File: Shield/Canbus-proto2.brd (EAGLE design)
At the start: 92.8 x 53 mm, 81 parts, among them J1 Digital_0_7, J2 Analog, J3 Digital_8_13, J4 Analog, J5 Digital_14_21

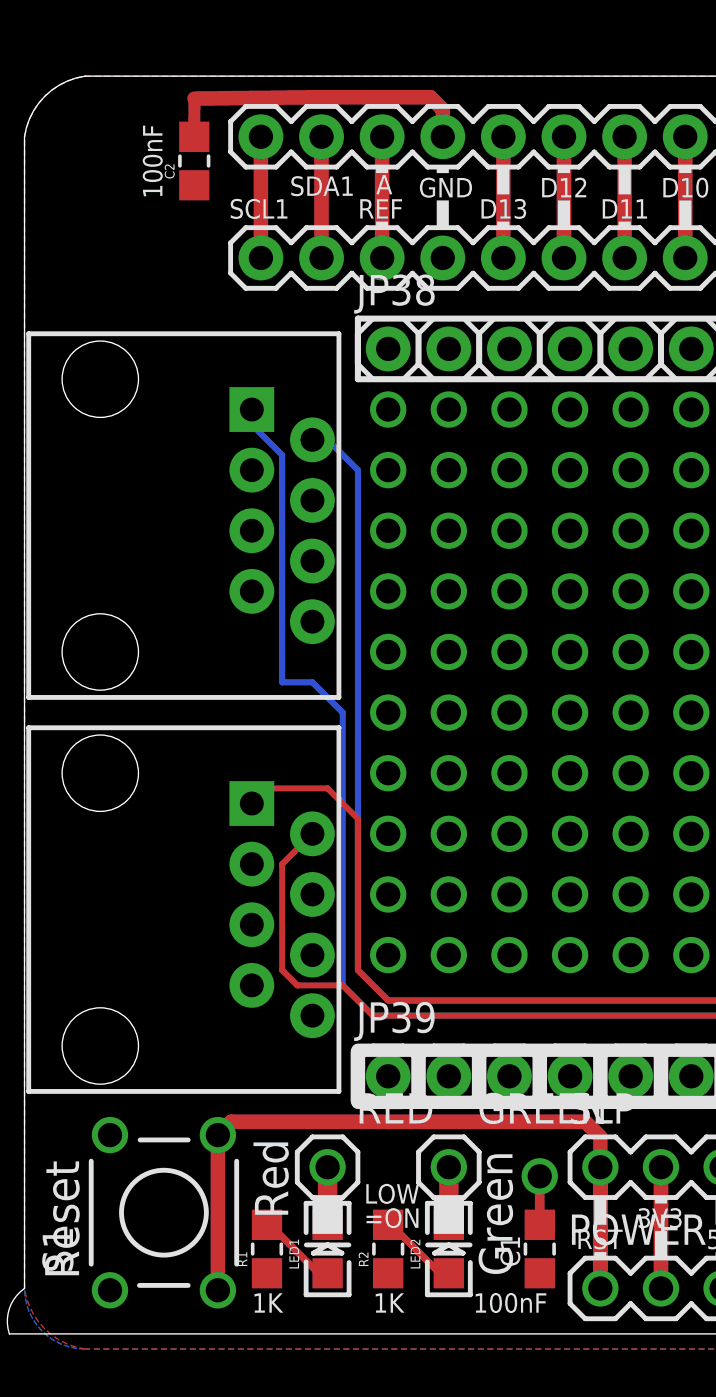
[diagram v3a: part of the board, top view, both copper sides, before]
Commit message: Switched all passives to 0603 to harmonize part sizes.
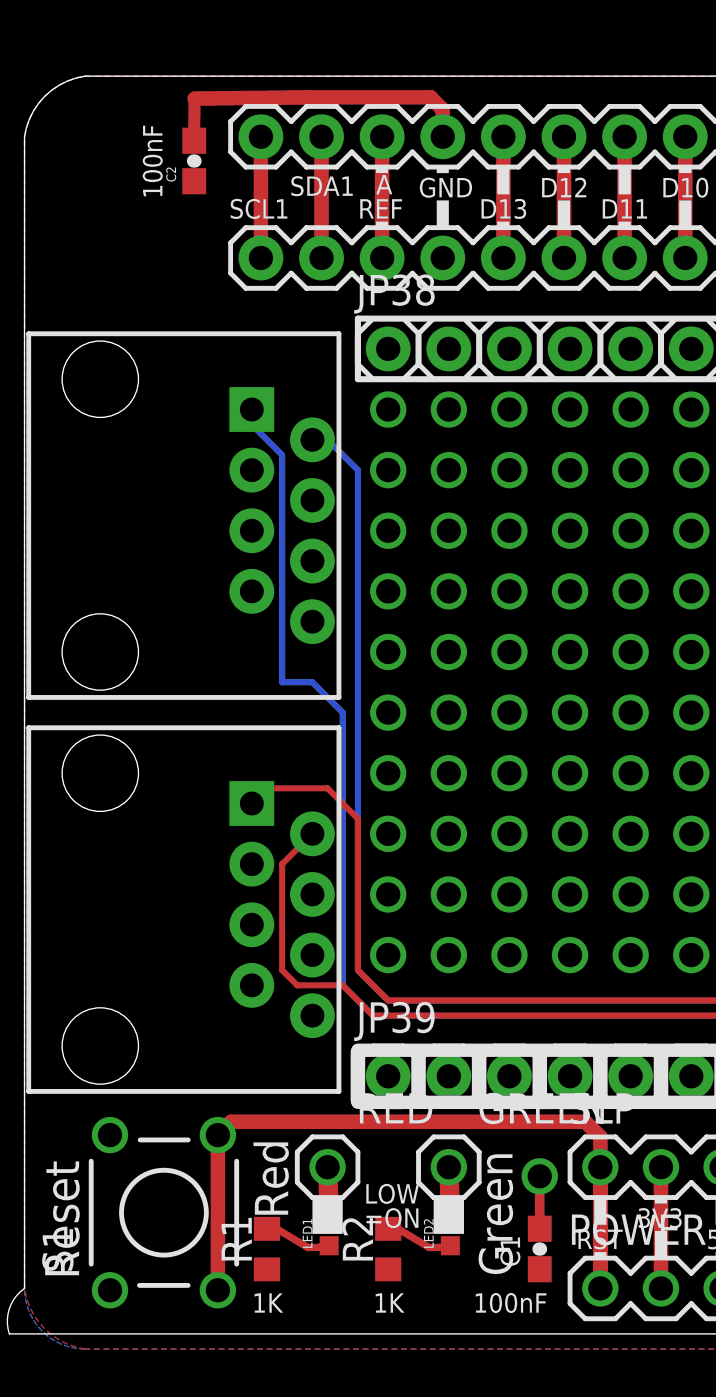
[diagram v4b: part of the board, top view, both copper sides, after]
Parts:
- C1, C2: value 100nF 0805 -> 100nF; device SparkFun:0805-LARGE -> SparkFun-Passives:0603-CAP
- LED1: value RED 0805 -> RED; device SparkFun:LED-0805-LARGE -> SparkFun-LED:LED-0603
- LED2: value GREEN 0805 -> GREEN; device SparkFun:LED-0805-LARGE -> SparkFun-LED:LED-0603
- R1, R2: value 1K 0805 -> 1K; device SparkFun:0805-LARGE -> rcl:R0603
- moved LED1 0.89 mm to (12.8, 5.08), turned to 0 degrees
- moved LED2 0.89 mm to (17.8, 5.08), turned to 0 degrees
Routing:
- net N$4: track 2.41 -> 1.79 mm
- net N$2: track 2.41 -> 1.79 mm
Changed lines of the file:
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@@
 <element name="SL3" library="SparkFun-Connectors" package="1X10" value="Digital_8_13" x="32.766" y="45.72" locked="yes" rot="R180"/>
 <element name="SL1" library="SparkFun" package="1X08" value="Digital_0_7" x="54.61" y="45.72" locked="yes" rot="R180"/>
-<element name="C1" library="SparkFun" package="0805-LARGE" value="100nF 0805" x="21.59" y="4.191" smashed="yes" rot="R90">
+<element name="C1" library="SparkFun-Passives" package="0603-CAP" value="100nF" x="21.59" y="4.191" smashed="yes" rot="R90">
 <attribute name="NAME" x="20.7645" y="3.429" size="0.8128" layer="25" ratio="13" rot="R90"/>
 <attribute name="VALUE" x="22.987" y="3.175" size="0.4064" layer="27" rot="R90"/>
 </element>
-<element name="C2" library="SparkFun" package="0805-LARGE" value="100nF 0805" x="7.112" y="49.784" rot="R90"/>
-<element name="LED1" library="SparkFun" package="LED-0805-LARGE" value="RED 0805" x="12.7" y="4.191" rot="R90"/>
-<element name="LED2" library="SparkFun" package="LED-0805-LARGE" value="GREEN 0805" x="17.78" y="4.191" rot="R90"/>
-<element name="R1" library="SparkFun" package="0805-LARGE" value="1K 0805" x="10.16" y="4.191" rot="R90"/>
-<element name="R2" library="SparkFun" package="0805-LARGE" value="1K 0805" x="15.24" y="4.191" rot="R90"/>
+<element name="C2" library="SparkFun-Passives" package="0603-CAP" value="100nF" x="7.112" y="49.784" rot="R90"/>
+<element name="LED1" library="SparkFun-LED" package="LED-0603" value="RED" x="12.7635" y="5.08">
+<attribute name="PROD_ID" value="DIO-00819" x="12.7635" y="5.08" size="1.778" layer="27" display="off"/>
+<attribute name="VALUE" value="RED" x="12.7635" y="5.08" size="1.778" layer="27" display="off"/>
+</element>
+<element name="LED2" library="SparkFun-LED" package="LED-0603" value="GREEN" x="17.8435" y="5.08">
+<attribute name="PROD_ID" value="DIO-00821" x="17.8435" y="5.08" size="1.778" layer="27" display="off"/>
+<attribute name="VALUE" value="GREEN" x="17.8435" y="5.08" size="1.778" layer="27" display="off"/>
+</element>
+<element name="R1" library="rcl" package="R0603" value="1K" x="10.16" y="4.191" rot="R90"/>
+<element name="R2" library="rcl" package="R0603" value="1K" x="15.24" y="4.191" rot="R90"/>
 <element name="S1" library="SparkFun" package="TACTILE-PTH" value="RESET" x="5.842" y="5.715" rot="R90"/>
 <element name="RED" library="SparkFun" package="1X01" value="" x="12.7" y="7.62"/>
@@
 <contactref element="JP36" pad="1"/>
 <contactref element="JP36" pad="10"/>
-<wire x1="21.59" y1="5.207" x2="21.59" y2="7.239" width="0.4064" layer="1"/>
-<wire x1="7.112" y1="50.8" x2="7.123" y2="52.3985" width="0.508" layer="1"/>
+<wire x1="21.59" y1="5.041" x2="21.59" y2="7.239" width="0.4064" layer="1"/>
+<wire x1="7.112" y1="50.634" x2="7.123" y2="52.3985" width="0.508" layer="1"/>
 <wire x1="7.123" y1="52.3985" x2="11.938" y2="52.451" width="0.6096" layer="1"/>
 <wire x1="11.938" y1="52.451" x2="17.018" y2="52.451" width="0.6096" layer="1"/>
@@
 <contactref element="R1" pad="2"/>
 <contactref element="LED1" pad="A"/>
-<wire x1="10.287" y1="5.207" x2="10.16" y2="5.207" width="0.3048" layer="1"/>
-<wire x1="12.192" y1="3.302" x2="10.287" y2="5.207" width="0.3048" layer="1"/>
-<wire x1="12.573" y1="3.302" x2="12.192" y2="3.302" width="0.3048" layer="1"/>
-<wire x1="12.573" y1="3.302" x2="12.7" y2="3.175" width="0.3048" layer="1"/>
+<wire x1="10.287" y1="5.207" x2="10.16" y2="5.041" width="0.3048" layer="1"/>
+<wire x1="11.8745" y1="4.2545" x2="10.287" y2="5.207" width="0.3048" layer="1"/>
+<wire x1="12.2555" y1="4.2545" x2="11.8745" y2="4.2545" width="0.3048" layer="1"/>
+<wire x1="12.2555" y1="4.2545" x2="12.7635" y2="4.33" width="0.3048" layer="1"/>
 </signal>
 <signal name="N$2">
 <contactref element="LED1" pad="C"/>
 <contactref element="RED" pad="1"/>
-<wire x1="12.7" y1="5.207" x2="12.7" y2="7.62" width="0.8128" layer="1"/>
+<wire x1="12.7635" y1="5.83" x2="12.7" y2="7.62" width="0.8128" layer="1"/>
 </signal>
 <signal name="N$3">
 <contactref element="R2" pad="2"/>
 <contactref element="LED2" pad="A"/>
-<wire x1="15.367" y1="5.207" x2="15.24" y2="5.207" width="0.3048" layer="1"/>
-<wire x1="17.272" y1="3.302" x2="15.367" y2="5.207" width="0.3048" layer="1"/>
-<wire x1="17.653" y1="3.302" x2="17.272" y2="3.302" width="0.3048" layer="1"/>
-<wire x1="17.653" y1="3.302" x2="17.78" y2="3.175" width="0.3048" layer="1"/>
+<wire x1="15.367" y1="5.207" x2="15.24" y2="5.041" width="0.3048" layer="1"/>
+<wire x1="16.9545" y1="4.2545" x2="15.367" y2="5.207" width="0.3048" layer="1"/>
+<wire x1="17.3355" y1="4.2545" x2="16.9545" y2="4.2545" width="0.3048" layer="1"/>
+<wire x1="17.3355" y1="4.2545" x2="17.8435" y2="4.33" width="0.3048" layer="1"/>
 </signal>
 <signal name="N$4">
 <contactref element="LED2" pad="C"/>
 <contactref element="GREEN" pad="1"/>
-<wire x1="17.78" y1="5.207" x2="17.78" y2="7.62" width="0.8128" layer="1"/>
+<wire x1="17.8435" y1="5.83" x2="17.78" y2="7.62" width="0.8128" layer="1"/>
 </signal>
 <signal name="A6">
@@
 <contactref element="JP38" pad="14"/>
 <contactref element="JP38" pad="15"/>
-<wire x1="15.24" y1="3.175" x2="15.24" y2="41.91" width="0" layer="19" extent="1-1"/>
+<wire x1="15.24" y1="3.341" x2="15.24" y2="41.91" width="0" layer="19" extent="1-1"/>
 </signal>
 <signal name="CAN0-EN">

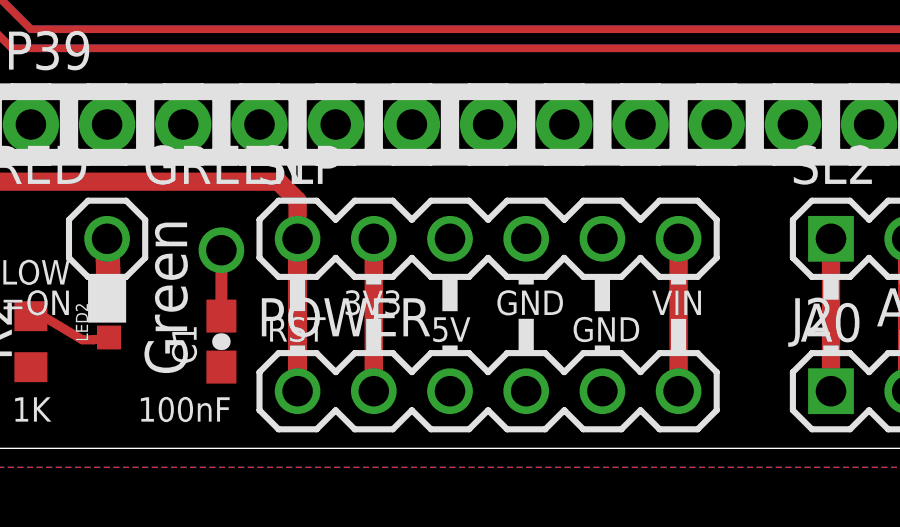
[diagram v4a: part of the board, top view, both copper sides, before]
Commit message: Slight component move on canbus Shield, drastic change to DueD to use ampseal and wifi layout
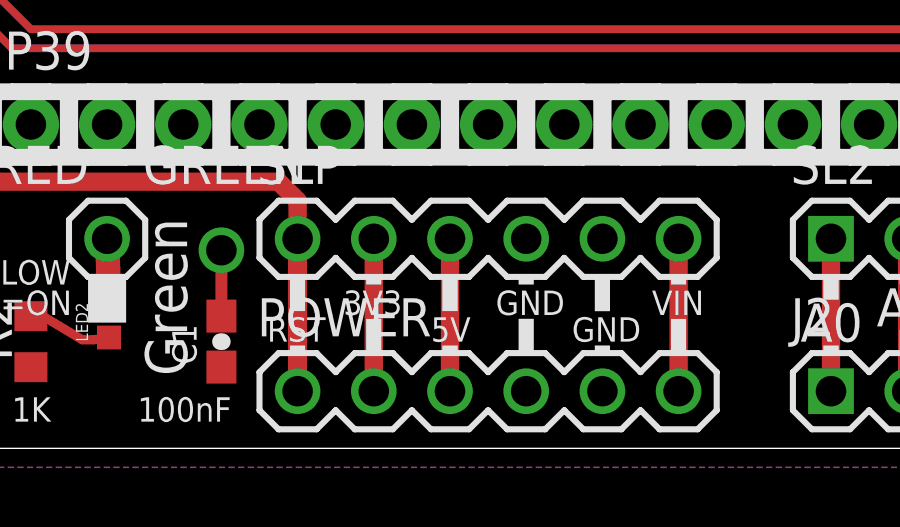
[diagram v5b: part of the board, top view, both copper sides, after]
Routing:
- net 5V: track 0.00 -> 5.08 mm
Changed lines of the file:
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@@
 <wire x1="85.09" y1="50.8" x2="87.63" y2="50.8" width="0" layer="19" extent="1-1"/>
 <wire x1="29.21" y1="7.62" x2="85.09" y2="50.8" width="0" layer="19" extent="1-1"/>
-<wire x1="29.21" y1="2.54" x2="29.21" y2="7.62" width="0" layer="19" extent="1-1"/>
+<wire x1="29.21" y1="7.62" x2="29.21" y2="2.54" width="0.6096" layer="1"/>
 </signal>
 <signal name="GND">

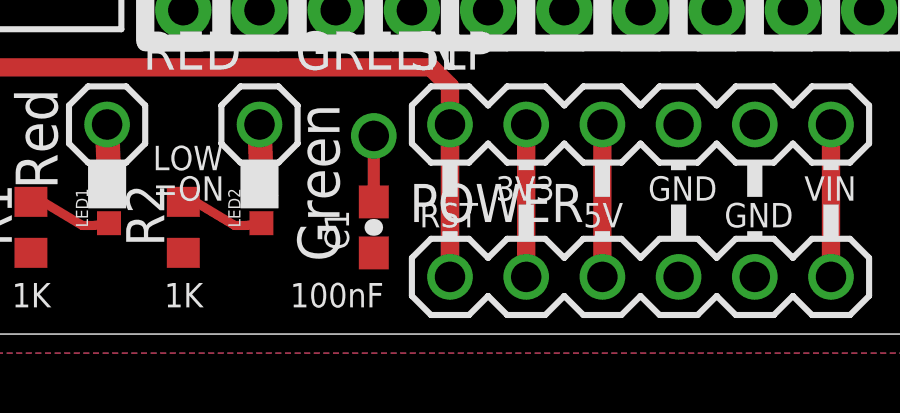
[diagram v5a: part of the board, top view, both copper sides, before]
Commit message: Updated canbus board to be more correct, fixed size of ampseal connector, totally new DueD board.
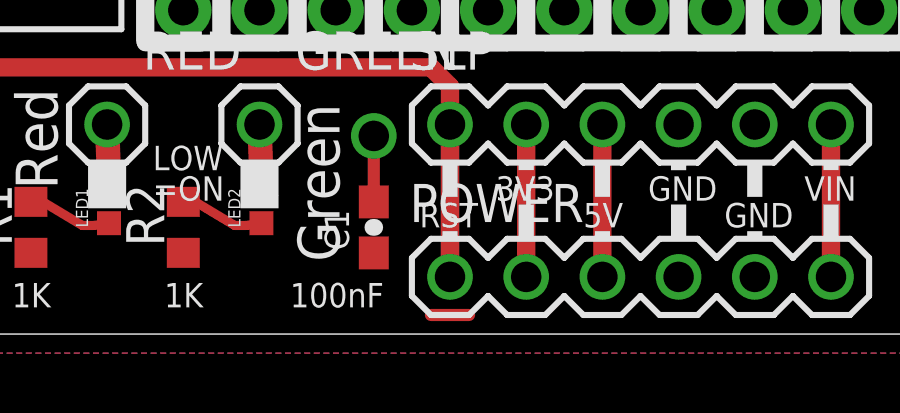
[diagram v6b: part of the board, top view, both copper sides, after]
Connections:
- removed net 3V3: POWER.2, SLP.2
- net +3V3: now also POWER.2, SLP.2
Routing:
- net +3V3: track 3.90 -> 10.2 mm
- net 3V3: track 5.08 -> 0.00 mm
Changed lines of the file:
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@@
 <wire x1="54.61" y1="2.54" x2="54.61" y2="7.62" width="0.6096" layer="1"/>
-</signal>
-<signal name="3V3">
-<contactref element="POWER" pad="2"/>
-<contactref element="SLP" pad="2"/>
-<wire x1="26.67" y1="2.54" x2="26.67" y2="7.62" width="0.6096" layer="1"/>
 </signal>
 <signal name="5V">
@@
 <contactref element="JP34" pad="2"/>
 <contactref element="JP34" pad="1"/>
+<wire x1="29.21" y1="7.62" x2="29.21" y2="2.54" width="0.6096" layer="1"/>
 <wire x1="85.09" y1="50.8" x2="87.63" y2="50.8" width="0" layer="19" extent="1-1"/>
 <wire x1="29.21" y1="7.62" x2="85.09" y2="50.8" width="0" layer="19" extent="1-1"/>
-<wire x1="29.21" y1="7.62" x2="29.21" y2="2.54" width="0.6096" layer="1"/>
 </signal>
 <signal name="GND">
@@
 <contactref element="JP38" pad="14"/>
 <contactref element="JP38" pad="15"/>
-<wire x1="15.24" y1="3.341" x2="15.24" y2="41.91" width="0" layer="19" extent="1-1"/>
+<contactref element="POWER" pad="2"/>
+<contactref element="SLP" pad="2"/>
+<wire x1="26.67" y1="2.54" x2="26.67" y2="7.62" width="0.6096" layer="1"/>
+<wire x1="23.495" y1="1.27" x2="24.765" y2="1.27" width="0.4064" layer="1"/>
+<wire x1="26.67" y1="2.54" x2="24.765" y2="1.27" width="0" layer="19" extent="1-1"/>
+<wire x1="21.59" y1="3.341" x2="23.495" y2="1.27" width="0" layer="19" extent="1-1"/>
 </signal>
 <signal name="CAN0-EN">

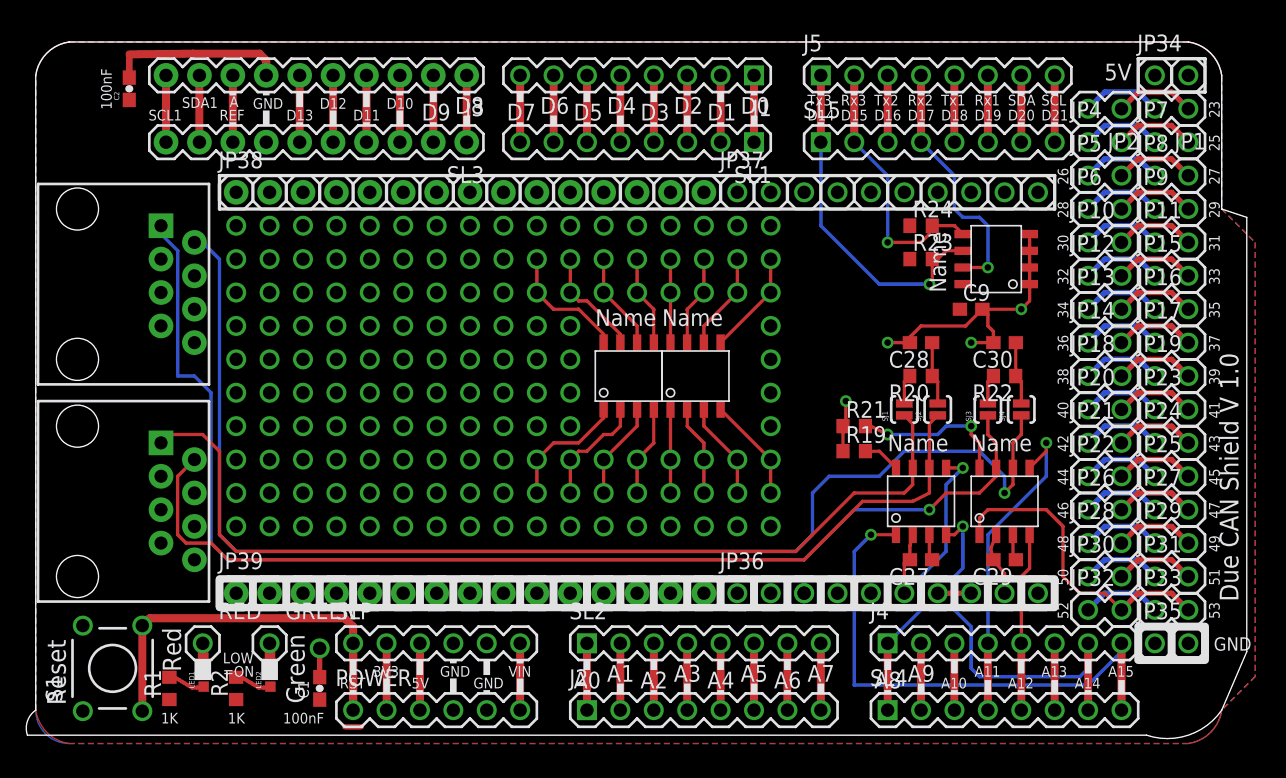
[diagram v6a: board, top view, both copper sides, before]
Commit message: Additional corrections and goodness for the shields.
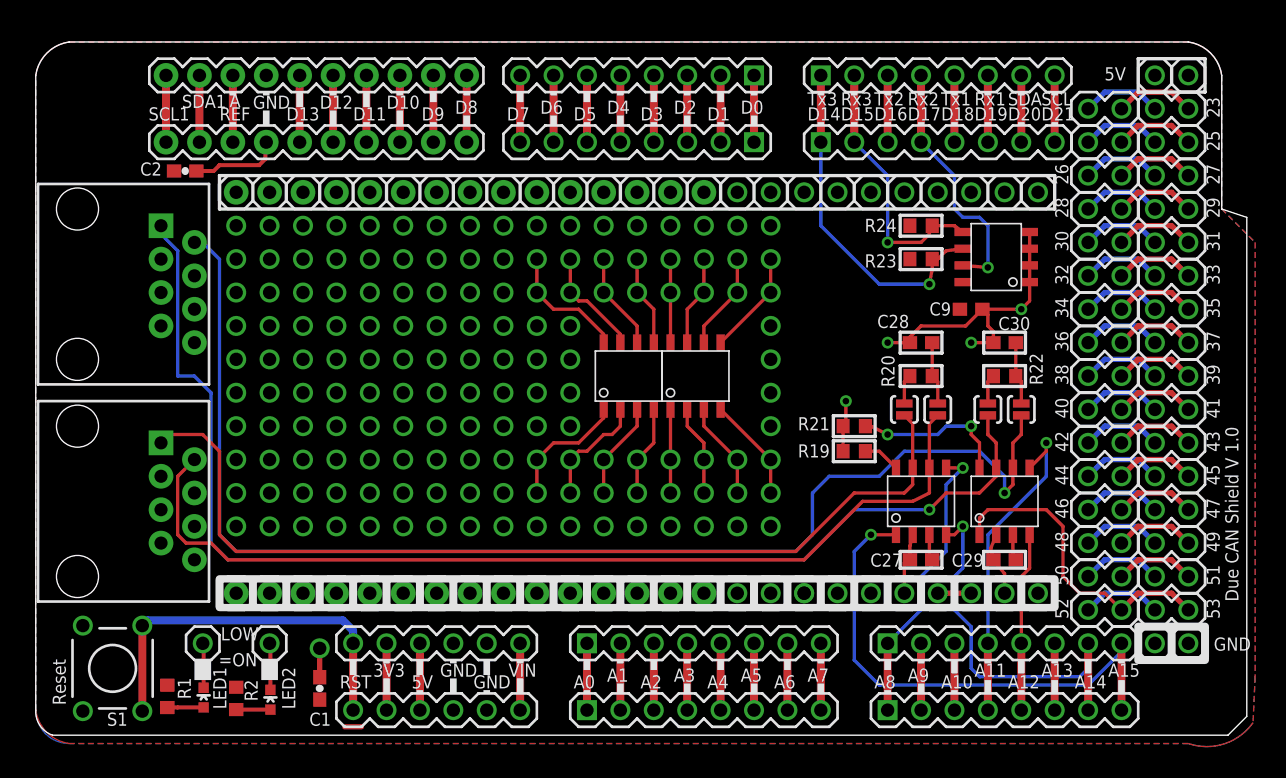
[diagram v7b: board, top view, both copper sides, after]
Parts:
- moved C2 7.56 mm to (11.4, 43.5), turned to 0 degrees
- moved LED2 1.75 mm to (17.8, 3.33)
- moved LED1 1.59 mm to (12.8, 3.49)
- moved R2 0.76 mm to (15.2, 3.43), turned to 270 degrees
- moved R1 0.62 mm to (10.0, 3.59), turned to 270 degrees
- moved U$6 0.16 mm to (74.9, 34.4)
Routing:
- net GND: track 54.2 -> 47.7 mm
- net RESET: track 34.5 -> 29.1 mm
- net N$4: track 1.79 -> 3.56 mm
- net N$2: track 1.79 -> 3.40 mm
- net CANTX0: track 40.9 -> 39.8 mm
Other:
- board size 92.8 x 53 mm -> 92.1 x 52.7 mm
- board text removed: "100nF"
- board text removed: "1K"
- board text removed: "Green"
- board text removed: "Red"
